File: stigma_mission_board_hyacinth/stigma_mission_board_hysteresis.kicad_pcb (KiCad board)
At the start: 4 copper layers, 70 x 120 mm, 166 parts, among them J1 DF40C-70DS-0.4V(51), J2 DF40HB(2.5)-10DS-0.4V(51), J7 SMA, J8 SMA, J9 JST-GH 4Pin, Q1 DMN2056U, Q2 DMN2056U, Q3 AOSP21321, Q8 DMN2056U, Q9 AOSP21321, U1 LAN8742A, U10 MCP2562-E-SN, U11 MCP2562-E-SN, U12 SN74HCS594, U13 INA181, U16 INA181, U2 INA181, U3 TPD4E1U06, U4 L7805, U5 L7805, U6 AZ1117H-ADJ, U7 AZ1117H-ADJ, U8 Ai-Thinker-Ra-01, U9 Ai-Thinker-Ra-01, Y1 25MHz

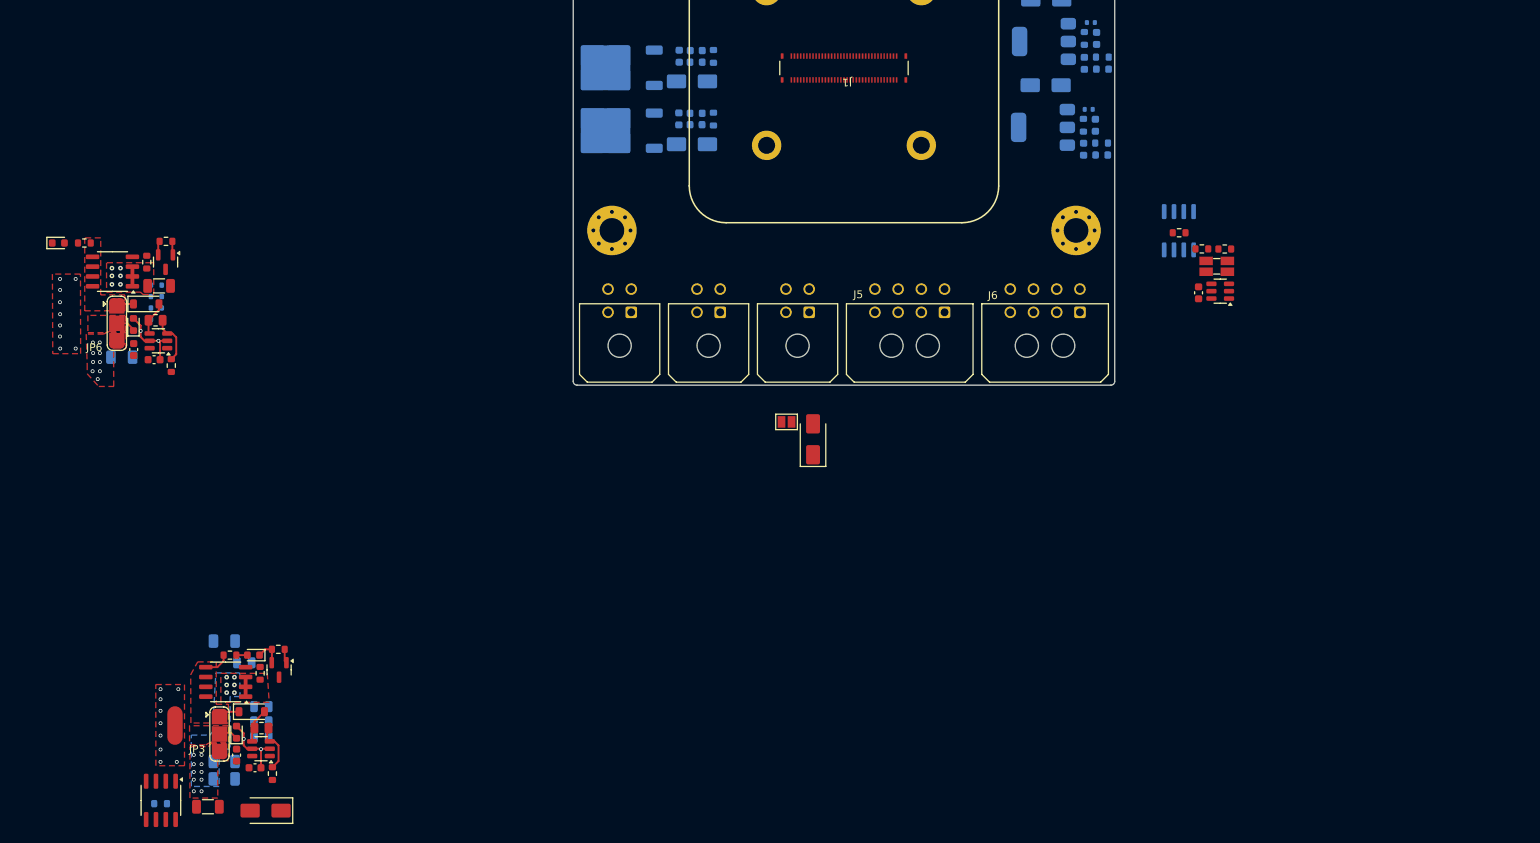
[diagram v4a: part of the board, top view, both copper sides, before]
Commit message: Rework recovery outputs to 2x2 low side
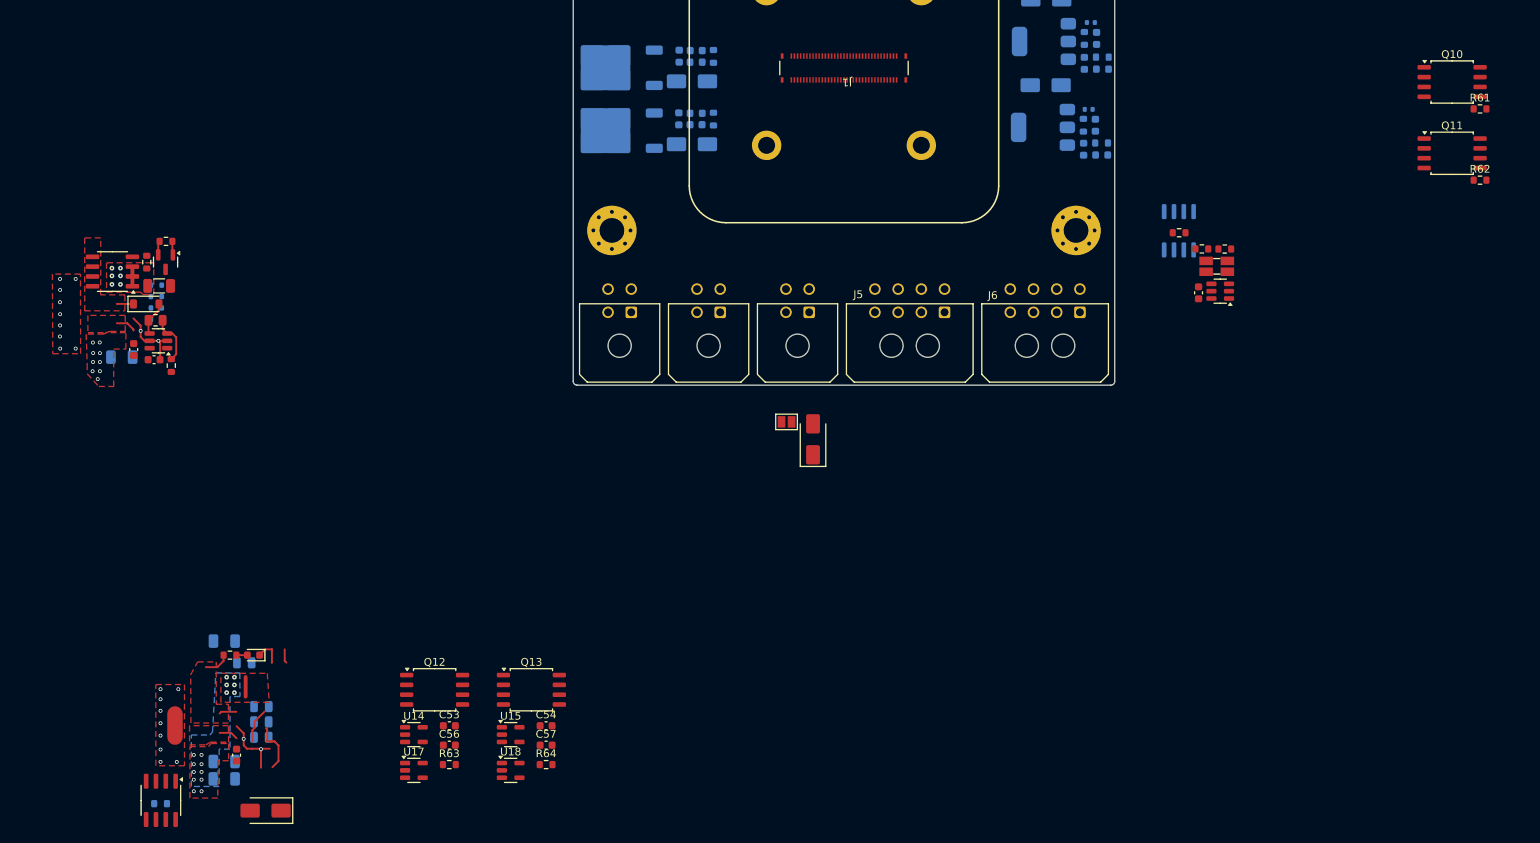
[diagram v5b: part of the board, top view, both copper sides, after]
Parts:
- removed C44: 10u, Capacitor_SMD:C_1206_3216Metric
- removed C45: 100n, Capacitor_SMD:C_0603_1608Metric
- removed D17: NRVB130T1G, Diode_SMD:D_SOD-123
- removed D19, D28: D, Diode_SMD:D_0603_1608Metric
- removed D27: LED, LED_SMD:LED_0603_1608Metric
- removed JP3, JP6: servo_switch, Stigma:SolderJumper-3_Open_RoundedPad2x2mm
- removed Q2: DMN2056U, Package_TO_SOT_SMD:SOT-23
- removed Q3: AOSP21321, Package_SO:SO-8_3.9x4.9mm_P1.27mm
- removed R45: 10k, Resistor_SMD:R_0603_1608Metric
- removed R46, R60: 1k, Resistor_SMD:R_0603_1608Metric
- removed R47: 60R, Resistor_SMD:R_0603_1608Metric
- removed Shunt1: 250mR 1%, Resistor_SMD:R_0805_2012Metric
- removed U13: INA181, Package_TO_SOT_SMD:SOT-23-6
- added C53: 100n, Capacitor_SMD:C_0603_1608Metric, F.Cu at (164.0, 291.0)
- added C54: 100n, Capacitor_SMD:C_0603_1608Metric, F.Cu at (176.5, 291.0)
- added C56: 100n, Capacitor_SMD:C_0603_1608Metric, F.Cu at (164.0, 293.5)
- added C57: 100n, Capacitor_SMD:C_0603_1608Metric, F.Cu at (176.5, 293.5)
- added Q10: TPH4R008NH, Package_SO:SSOP-8_5.25x5.24mm_P1.27mm, F.Cu at (293.6, 207.8)
- added Q11: TPH4R008NH, Package_SO:SSOP-8_5.25x5.24mm_P1.27mm, F.Cu at (293.6, 217.0)
- added Q12: TPH4R008NH, Package_SO:SSOP-8_5.25x5.24mm_P1.27mm, F.Cu at (162.1, 286.4)
- added Q13: TPH4R008NH, Package_SO:SSOP-8_5.25x5.24mm_P1.27mm, F.Cu at (174.6, 286.4)
- added R61: 10k, Resistor_SMD:R_0603_1608Metric, F.Cu at (297.2, 211.3)
- added R62: 10k, Resistor_SMD:R_0603_1608Metric, F.Cu at (297.2, 220.5)
- added R63: 10k, Resistor_SMD:R_0603_1608Metric, F.Cu at (164.0, 296.1)
- added R64: 10k, Resistor_SMD:R_0603_1608Metric, F.Cu at (176.5, 296.1)
- added U14: TF0216, Package_TO_SOT_SMD:SOT-23-5, F.Cu at (159.4, 292.2)
- added U15: TF0216, Package_TO_SOT_SMD:SOT-23-5, F.Cu at (171.9, 292.2)
- added U17: TF0216, Package_TO_SOT_SMD:SOT-23-5, F.Cu at (159.4, 296.8)
- added U18: TF0216, Package_TO_SOT_SMD:SOT-23-5, F.Cu at (171.9, 296.8)
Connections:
- net ADC_RECOVERY_1_I renamed ADC_RECOVERY
- net ADC_RECOVERY_2_I renamed RECOVERY_CONT_CHECK
- C50 pad 1: /Recovery Output 1/high_current -> high_current
- D26 pad 1: /Recovery Output 1/recovery_switched -> /recovery_high
- F1 pad 1: /Recovery Output 1/high_current -> Net-(Q12-D)
- F1 pad 2: high_current -> Net-(J10-Pin_1)
- F2 pad 1: /Recovery Output3/high_current -> Net-(Q13-D)
- F2 pad 2: high_current -> Net-(J13-Pin_1)
- F3 pad 1: /Recovery Output 1/high_current -> Net-(Q10-D)_1
- F3 pad 2: +5V -> Net-(J10-Pin_2)
- F4 pad 1: /Recovery Output3/high_current -> Net-(Q11-D)
- F4 pad 2: +5V -> Net-(J13-Pin_2)
- J1 pad 14: RECOVERY_1_CONT_CHECK -> RECOVERY_SWITCH
- J1 pad 15: RECOVERY_2_CONT_CHECK -> unconnected-(J1-Pin_15-Pad15)
- J1 pad 16: RECOVERY_3_CONT_CHECK -> unconnected-(J1-Pin_16-Pad16)
- J1 pad 17: RECOVERY_4_CONT_CHECK -> unconnected-(J1-Pin_17-Pad17)
- Q8 pad 1: RECOVERY_1 -> RECOVERY_SWITCH
- Q9 pad 1: /Recovery Output 1/high_current -> high_current
- Q9 pad 2: /Recovery Output 1/high_current -> high_current
- Q9 pad 3: /Recovery Output 1/high_current -> high_current
- Q9 pad 5: /Recovery Output 1/recovery_switched -> /recovery_high
- Q9 pad 6: /Recovery Output 1/recovery_switched -> /recovery_high
- Q9 pad 7: /Recovery Output 1/recovery_switched -> /recovery_high
- Q9 pad 8: /Recovery Output 1/recovery_switched -> /recovery_high
- R48 pad 1: /Recovery Output3/recovery_switched -> /recovery_high
- R57 pad 1: RECOVERY_1 -> RECOVERY_SWITCH
- R58 pad 1: /Recovery Output 1/high_current -> high_current
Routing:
- net (no net): track 0.00 -> 14.0 mm
- net Net-(U13-+): track 6.92 -> 0.00 mm
- net /recovery_high: track 0.00 -> 5.53 mm
- net Net-(D17-A): track 4.50 -> 0.00 mm
- net /Recovery Output 1/servo_line: track 2.63 -> 0.00 mm
- net high_current: track 0.00 -> 2.54 mm, vias 0 -> 15
- net /Recovery Output 1/high_current: track 2.54 -> 0.00 mm, vias 15 -> 0
- net /Recovery Output3/high_current: track 2.54 -> 0.00 mm, vias 16 -> 0
- net /Recovery Output3/servo_line: track 2.48 -> 0.00 mm
- net RECOVERY_SWITCH: track 0.00 -> 1.77 mm
- net RECOVERY_1: track 1.77 -> 0.00 mm
- net /Recovery Output3/recovery_switched: track 5.64 -> 4.73 mm
- net Net-(Q11-D): vias 0 -> 16
- added copper zone on F.Cu, net /recovery_high
- added copper zone on B.Cu, net Net-(Q11-D)
- added copper zone on F.Cu, net Net-(Q11-D)
- added copper zone on F.Cu, net high_current
- removed copper zone on F.Cu, net /Recovery Output 1/high_current
- removed copper zone on F.Cu, net /Recovery Output 1/recovery_switched
- removed copper zone on F.Cu, net /Recovery Output 1/servo_line
- removed copper zone on B.Cu, net /Recovery Output3/high_current
- removed copper zone on F.Cu, net /Recovery Output3/high_current
- removed copper zone on F.Cu, net /Recovery Output3/recovery_switched
- removed copper zone on F.Cu, net /Recovery Output3/servo_line

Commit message: Refactor schematic, esp. recovery outputs, prepare for final layout
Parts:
- removed C14, C15: 10u, Capacitor_SMD:C_0603_1608Metric
- removed C20, C21: 22u, Capacitor_SMD:C_0603_1608Metric
- removed C42: C, Capacitor_SMD:C_0603_1608Metric
- removed C50: 10u, Capacitor_SMD:C_1206_3216Metric
- removed D10, D9: SS34, Diode_SMD:D_SMA
- removed D11, D12: red, LED_SMD:LED_0603_1608Metric
- removed J10, J4: ~, Connector_Molex:Molex_Micro-Fit_3.0_43045-0400_2x02_P3.00mm_Horizontal
- removed JP2: SolderJumper_2_Open, Jumper:SolderJumper-2_P1.3mm_Open_Pad1.0x1.5mm
- removed R12: 100mR 1%, Resistor_SMD:R_Shunt_Ohmite_LVK12
- removed R18, R24: 10k, Resistor_SMD:R_0603_1608Metric
- removed R23: 100k, Resistor_SMD:R_0603_1608Metric
- removed R30, R32: 150R, Resistor_SMD:R_0603_1608Metric
- removed R31, R33: 310R, Resistor_SMD:R_0402_1005Metric
- removed R36, R37: 220, Resistor_SMD:R_0603_1608Metric
- removed RJ1: ~, Stigma:RJ45-TH_MJ88B-B011-RVL11-P
- removed Shunt4: 250mR 1%, Resistor_SMD:R_0805_2012Metric
- removed U6, U7: AZ1117H-ADJ, Package_TO_SOT_SMD:SOT-223-3_TabPin2
- added C37: 10u, Capacitor_SMD:C_0603_1608Metric, F.Cu at (357.9, 347.4)
- added C38: 22u, Capacitor_SMD:C_0603_1608Metric, F.Cu at (357.9, 349.9)
- added C39: 10u, Capacitor_SMD:C_0603_1608Metric, F.Cu at (418.7, 66.9)
- added C44: 10u, Capacitor_SMD:C_0603_1608Metric, F.Cu at (162.1, 106.6)
- added C45: 10u, Capacitor_SMD:C_0603_1608Metric, F.Cu at (275.2, 128.8)
- added C46: 22u, Capacitor_SMD:C_0603_1608Metric, F.Cu at (175.2, 119.3)
- added C47: 22u, Capacitor_SMD:C_0603_1608Metric, F.Cu at (263.9, 121.6)
- added C58: 100n, Capacitor_SMD:C_0603_1608Metric, F.Cu at (30.3, 195.4)
- added C59: 100n, Capacitor_SMD:C_0603_1608Metric, F.Cu at (290.7, 260.0)
- added C60: 100n, Capacitor_SMD:C_0603_1608Metric, F.Cu at (290.7, 262.5)
- added C61: 100n, Capacitor_SMD:C_0603_1608Metric, F.Cu at (290.7, 265.1)
- added C62: 100n, Capacitor_SMD:C_0603_1608Metric, F.Cu at (290.7, 267.6)
- added D21: red, LED_SMD:LED_0603_1608Metric, F.Cu at (139.2, 309.7)
- added D22: red, LED_SMD:LED_0603_1608Metric, F.Cu at (139.2, 312.3)
- added F5: PTC?, Fuse:Fuse_1206_3216Metric, F.Cu at (144.8, 302.4)
- added J11: JST-GH, Connector_JST:JST_GH_BM04B-GHS-TBT_1x04-1MP_P1.25mm_Vertical, F.Cu at (407.1, 286.2)
- added J3: RJ45_Wuerth_7499010211A, Connector_RJ:RJ45_Wuerth_7499010211A_Horizontal, F.Cu at (218.5, 137.2)
- added R56: 10k, Resistor_SMD:R_0603_1608Metric, F.Cu at (144.8, 314.0)
- added R60: 1k, Resistor_SMD:R_0603_1608Metric, F.Cu at (42.4, 205.5)
- added R65: 220, Resistor_SMD:R_0603_1608Metric, F.Cu at (42.4, 208.0)
- added R66: 1k, Resistor_SMD:R_0603_1608Metric, F.Cu at (42.4, 210.5)
- added R67: 220, Resistor_SMD:R_0603_1608Metric, F.Cu at (42.4, 213.0)
- added R68: 1k, Resistor_SMD:R_0603_1608Metric, F.Cu at (42.4, 215.5)
- added R69: 10k, Resistor_SMD:R_0603_1608Metric, F.Cu at (46.4, 185.4)
- added R70: 22, Resistor_SMD:R_0603_1608Metric, F.Cu at (415.2, 272.0)
- added R71: 270, Resistor_SMD:R_0603_1608Metric, F.Cu at (452.4, 50.3)
- added R72: 22, Resistor_SMD:R_0603_1608Metric, F.Cu at (415.2, 277.0)
- added R73: 22, Resistor_SMD:R_0603_1608Metric, F.Cu at (415.2, 279.5)
- added R74: 22, Resistor_SMD:R_0603_1608Metric, F.Cu at (415.2, 282.0)
- added U13: AZ1117I-3.3, Package_TO_SOT_SMD:SOT-223-3_TabPin2, F.Cu at (407.8, 55.6)
- added U19: AZ1117I-3.3, Package_TO_SOT_SMD:SOT-223-3_TabPin2, F.Cu at (157.5, 114.8)
- added U20: AZ1117I-3.3, Package_TO_SOT_SMD:SOT-223-3_TabPin2, F.Cu at (263.9, 131.8)
- C16, C17, C18, C19, C31, C33, C34, C52, D1, D2, D3, D4, D5, D6, D7, D8, F1, F2, F3, F4, R41, U4, U5: moved to F.Cu
- C43: value 100n -> 22u
- D18: value LED -> yellow
- J13: footprint Connector_Molex:Molex_Micro-Fit_3.0_43045-0400_2x02_P3.00mm_Horizontal -> Connector_Molex:Molex_Micro-Fit_3.0_43045-1200_2x06_P3.00mm_Horizontal
- J9: value JST-GH 4Pin -> JST-GH
- R1, R2, R4: value 33R -> 33
- R28: value 270 -> 100k
- R34, R35: value 220 -> 1k; moved to F.Cu
- R42: value R -> 10k
- R44: value @todo -> 220
- R48: value 1k -> 10k
- R59: value 60R -> 1k
- U10: value MCP2562-E-SN -> MCP2562; moved to F.Cu
- U11: value MCP2562-E-SN -> MCP2562
- U12: value SN74HCS594 -> AZ1117I-3.3; footprint Package_SO:TSSOP-16_4.4x5mm_P0.65mm -> Package_TO_SOT_SMD:SOT-223-3_TabPin2
- moved C43 289.5 mm to (418.7, 69.4), turned to 0 degrees
- moved U12 287.2 mm to (346.9, 332.8)
- moved Q10 235.8 mm to (58.6, 187.5)
- moved Q11 235.2 mm to (58.6, 206.1)
- moved R61 232.3 mm to (65.9, 190.4)
- moved R62 231.6 mm to (65.9, 209.0)
- moved C40 213.7 mm to (123.2, 324.1)
- moved C35 212.8 mm to (128.7, 316.5)
- moved Q1 209.5 mm to (445.1, 209.2), turned to 0 degrees
- moved R28 209.4 mm to (201.2, 323.2), turned to 0 degrees
- moved C32 207.0 mm to (123.2, 315.1)
- moved R44 206.6 mm to (443.1, 204.4), turned to 0 degrees
- moved D16 203.9 mm to (439.0, 210.3), turned to 0 degrees
- moved R43 203.3 mm to (443.1, 201.9)
- moved C30 203.3 mm to (123.2, 309.1)
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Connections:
- net CAN_1_RX renamed CAN1_RX
- net CAN_1_TX renamed CAN1_TX
- net CAN_2_RX renamed CAN2_RX
- net CAN_2_TX renamed CAN2_TX
- net ETH_TXD0 renamed ETH_TXD-
- net ETH_TXD1 renamed ETH_TXD+
- net HSE_IN renamed Net-(U1-XTAL1/CLKIN)
- net HSE_OUT renamed Net-(U1-XTAL2)
- net LoRa_1_BUSY renamed LORA1_BUSY
- net LoRa_1_IRQ renamed LORA1_IRQ
- net LoRa_1_NSS renamed LORA1_CS
- net LoRa_2_BUSY renamed LORA2_BUSY
- net LoRa_2_IRQ renamed LORA2_IRQ
- net RECOVERY_1 renamed RECOVERY_LOW1
- net RECOVERY_1_CONT_CHECK renamed Net-(Q2-S)
- net RECOVERY_2 renamed RECOVERY_LOW2
- net RECOVERY_3 renamed RECOVERY_LOW3
- net RECOVERY_4 renamed RECOVERY_LOW4
- net TELEMETRIE_SPI4_MISO renamed LORA_SPI4_MISO
- net TELEMETRIE_SPI4_MOSI renamed LORA_SPI4_MOSI
- net TELEMETRIE_SPI4_SCK renamed LORA_SPI4_SCK
- C16 pad 2: main_voltage -> main
- C17 pad 2: main_voltage -> main
- C26 pad 2: +3.3V -> vdd_lora1
- C27 pad 2: +3.3V -> vdd_lora2
- C28 pad 2: +3.3V -> vdd_lora1
- C29 pad 2: +3.3V -> vdd_lora2
- C3 pad 1: +3.3V -> vdd_ethernet
- C30 pad 2: main_voltage -> main
- C31 pad 2: high_current -> recovery
- C32 pad 2: main_voltage -> main
- C33 pad 2: high_current -> recovery
- C34 pad 2: high_current -> recovery
- C35 pad 2: main_voltage -> main
- C36 pad 2: high_current -> recovery
- C40 pad 2: main_voltage -> main
- C43 pad 2: +3.3V -> vdd_ethernet
- C51 pad 1: +3.3V -> GND
- C51 pad 2: GND -> +3.3V
- C52 pad 2: high_current -> recovery
- C55 pad 2: high_current -> recovery
- D14 pad 1: v_main_pre_sense -> main_pre_sense
- D14 pad 2: Net-(D14-A) -> bus_main
- D15 pad 1: v_main_pre_sense -> main_pre_sense
- D15 pad 2: Net-(D15-A) -> recovery
- D26 pad 1: /recovery_high -> Net-(D26-K)
- D3 pad 1: SR_GPS_RESET -> GPS_RESET
- D4 pad 1: SR_GPS_SAFEBOOT -> GPS_SAFEBOOT
- F1 pad 1: Net-(Q12-D) -> Net-(D19-K)
- F1 pad 2: Net-(J10-Pin_1) -> Net-(Q12-D)
- F2 pad 1: Net-(Q13-D) -> Net-(D20-K)
- F2 pad 2: Net-(J13-Pin_1) -> Net-(Q13-D)
- FB1 pad 1: +3.3V -> vdd_ethernet
- J1 pad 11: SR1_SER -> LORA1_RESET
- J1 pad 12: SR1_SRCLK -> LORA2_CS
- J1 pad 13: SR1_RCLK -> LORA2_RESET
- J1 pad 14: RECOVERY_SWITCH -> GPS_RESET
- J1 pad 15: unconnected-(J1-Pin_15-Pad15) -> GPS_SAFEBOOT
- J1 pad 16: unconnected-(J1-Pin_16-Pad16) -> RECOVERY_HIGH
- J1 pad 17: unconnected-(J1-Pin_17-Pad17) -> CONT_CHECK
- J1 pad 23: SPI3_SCK_PC10 -> unconnected-(J1-Pin_23-Pad23)
- J1 pad 24: SPI3_MISO_PC11 -> unconnected-(J1-Pin_24-Pad24)
- J1 pad 25: SPI3_MOSI_PC12 -> unconnected-(J1-Pin_25-Pad25)
- J1 pad 28: ADC_HIGH_CURRENT -> ADC_IN
- J1 pad 29: ADC_HIGH_CURRENT2 -> ETH_RESET
- J1 pad 4: LoRa_2_NSS -> UART8_RX
- J1 pad 46: ADC_RECOVERY -> ADC_BUS_MAIN_VOLTAGE
- J1 pad 47: RECOVERY_CONT_CHECK -> ADC_BUS_SUPPLY_VOLTAGE
- J1 pad 5: ETH_nINT -> UART8_TX
- J1 pad 59: ADC_RECOVERY_3_I -> ADC_MAIN_CURRENT
- J1 pad 62: ADC_RECOVERY_4_I -> ADC_RECOVERY_VOLTAGE
- J1 pad 65: ADC_MAIN_VOLTAGE_CURRENT -> ADC_RECOVERY_CURRENT
- J1 pad 67: ADC_MAIN_VOLTAGE -> ADC_CONT_CHECK
- J2 pad 6: SR_GPS_SAFEBOOT -> GPS_SAFEBOOT
- J2 pad 7: SR_GPS_RESET -> GPS_RESET
- J9 pad 2: DAC -> Net-(J9-Pin_2)
- J9 pad 3: GND -> Net-(J9-Pin_3)
- Q8 pad 1: RECOVERY_SWITCH -> Net-(Q8-G)
- Q9 pad 1: high_current -> recovery
- Q9 pad 2: high_current -> recovery
- Q9 pad 3: high_current -> recovery
- Q9 pad 5: /recovery_high -> Net-(D26-K)
- Q9 pad 6: /recovery_high -> Net-(D26-K)
- Q9 pad 7: /recovery_high -> Net-(D26-K)
- Q9 pad 8: /recovery_high -> Net-(D26-K)
- R1 pad 2: ETH_RXD0 -> ETH_RXD-
- R10 pad 2: +3.3V -> vdd_ethernet
- R11 pad 2: +3.3V -> vdd_ethernet
- R19 pad 1: v_main_pre_sense -> bus_main
- R19 pad 2: ADC_MAIN_VOLTAGE -> ADC_BUS_MAIN_VOLTAGE
- R2 pad 2: ETH_RXD1 -> ETH_RXD+
- R20 pad 1: ADC_MAIN_VOLTAGE -> ADC_BUS_MAIN_VOLTAGE
- R22 pad 1: ETH_nINT -> Net-(U1-LED2/~{INTSEL})
- R25 pad 1: high_current -> bus_supply
- R25 pad 2: ADC_HIGH_CURRENT -> ADC_BUS_SUPPLY_VOLTAGE
- R26 pad 1: ADC_HIGH_CURRENT -> ADC_BUS_SUPPLY_VOLTAGE
- R28 pad 1: Net-(RJ1-L-) -> recovery
- R28 pad 2: GND -> ADC_RECOVERY_VOLTAGE
- R40 pad 1: CAN_1_H -> CAN1+
- R40 pad 2: CAN_1_L -> CAN1-
- R41 pad 1: CAN_2_H -> CAN2+
- R41 pad 2: CAN_2_L -> CAN2-
- R42 pad 1: +3.3V -> ADC_RECOVERY_VOLTAGE
- R42 pad 2: Net-(U12-~{RCLR}) -> GND
- R48 pad 1: /recovery_high -> /Recovery Output 1 & 2/recovery_high
- R57 pad 1: RECOVERY_SWITCH -> recovery
- R57 pad 2: GND -> Net-(D22-A)
- R58 pad 1: high_current -> recovery
- R59 pad 2: Net-(U16-+) -> Net-(R59-Pad2)
- R6 pad 1: SR_ETH_RESET -> Net-(U1-~{INT}/REFCLKO)
- R6 pad 2: +3.3V -> vdd_ethernet
- R8 pad 2: +3.3V -> vdd_ethernet
- R9 pad 2: +3.3V -> vdd_ethernet
- U1 pad 15: SR_ETH_RESET -> ETH_RESET
- U1 pad 2: ETH_nINT -> Net-(U1-LED2/~{INTSEL})
- U1 pad 9: +3.3V -> vdd_ethernet
- U10 pad 6: CAN_1_L -> CAN1-
- U10 pad 7: CAN_1_H -> CAN1+
- U10 pad 8: SR_CAN_STBY_1 -> GND
- U11 pad 6: CAN_2_L -> CAN2-
- U11 pad 7: CAN_2_H -> CAN2+
- U11 pad 8: SR_CAN_STBY_2 -> GND
- U12 pad 1: SR_CAN_STBY_2 -> GND
- U12 pad 2: SR_ETH_RESET -> +3.3V
- U12 pad 3: SR_LoRa_1_RESET -> +5V
- U16 pad 1: ADC_RECOVERY -> ADC_RECOVERY_CURRENT
- U16 pad 3: Net-(U16-+) -> Net-(D26-K)
- U16 pad 4: Net-(D26-A) -> /Recovery Output 1 & 2/recovery_high
- U2 pad 1: ADC_MAIN_VOLTAGE_CURRENT -> ADC_MAIN_CURRENT
- U2 pad 3: Net-(U2-+) -> main_pre_sense
- U2 pad 4: Net-(U2--) -> main
- U3 pad 4: /RXP -> /RXN
- U3 pad 5: /RXN -> /RXP
- U4 pad 1: main_voltage -> main
- U5 pad 1: main_voltage -> main
- U8 pad 3: +3.3V -> vdd_lora1
- U8 pad 4: SR_LoRa_1_RESET -> LORA1_RESET
- U9 pad 15: LoRa_2_NSS -> LORA2_CS
- U9 pad 3: +3.3V -> vdd_lora2
- U9 pad 4: SR_LoRa_2_RESET -> LORA2_RESET
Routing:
- net GND: track 26.5 -> 0.00 mm, vias 22 -> 0
- net (no net): track 14.0 -> 0.00 mm
- net Net-(U16-+): track 6.41 -> 0.00 mm
- net /recovery_high: track 5.53 -> 0.00 mm
- net /Recovery Output3/recovery_switched: track 4.73 -> 0.00 mm
- net Net-(D26-A): track 4.44 -> 0.00 mm
- net /Recovery Output 1/recovery_switched: track 2.63 -> 0.00 mm
- net high_current: track 2.54 -> 0.00 mm, vias 15 -> 0
- net RECOVERY_LOW3: track 1.82 -> 0.00 mm
- net RECOVERY_SWITCH: track 1.77 -> 0.00 mm
- net Net-(D18-A): track 1.43 -> 0.00 mm
- net Net-(Q11-D): vias 16 -> 0
- removed copper zone on F.Cu, net /recovery_high
- removed copper zone on F.Cu, net GND
- removed copper zone on B.Cu, net Net-(Q11-D)
- removed copper zone on F.Cu, net Net-(Q11-D)
- removed copper zone on F.Cu, net high_current
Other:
- outline, holes or cut-outs redrawn
- board text removed: "3,3V"
- board text removed: "5V Regulator"
- board text removed: "BZR"
- board text removed: "Ethernet"
- board text removed: "see what we do with those"
- board text removed: "sensing"
- board text removed: "shift"

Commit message: start routing
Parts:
- removed C56, C57, C58, C59, C60, C61, C62: 100n, Capacitor_SMD:C_0603_1608Metric
- removed D14: SS34, Diode_SMD:D_SMA
- removed D21, D22: red, LED_SMD:LED_0603_1608Metric
- removed D26: NRVB130T1G, Diode_SMD:D_SOD-123
- removed J11: JST-GH, Connector_JST:JST_GH_BM04B-GHS-TBT_1x04-1MP_P1.25mm_Vertical
- removed J13: ~, Connector_Molex:Molex_Micro-Fit_3.0_43045-1200_2x06_P3.00mm_Horizontal
- removed Q10, Q11, Q12, Q13: TPH4R008NH, Package_SO:SSOP-8_5.25x5.24mm_P1.27mm
- removed Q9: AOSP21321, Package_SO:SO-8_3.9x4.9mm_P1.27mm
- removed R67: 220, Resistor_SMD:R_0603_1608Metric
- removed R68: 1k, Resistor_SMD:R_0603_1608Metric
- removed R69: 10k, Resistor_SMD:R_0603_1608Metric
- removed R70, R72, R73, R74: 22, Resistor_SMD:R_0603_1608Metric
- removed R71: 270, Resistor_SMD:R_0603_1608Metric
- removed U19, U20: AZ1117I-3.3, Package_TO_SOT_SMD:SOT-223-3_TabPin2
- added C14: 100n, Capacitor_SMD:C_0402_1005Metric, F.Cu at (204.3, 222.3)
- added C15: 10u, Capacitor_SMD:C_0603_1608Metric, F.Cu at (165.3, 172.5)
- added C20: 1u, Capacitor_SMD:C_0402_1005Metric, F.Cu at (192.9, 235.0)
- added C21: 10u, Capacitor_SMD:C_0603_1608Metric, F.Cu at (160.5, 233.2)
- added C41: 1u, Capacitor_SMD:C_0402_1005Metric, F.Cu at (176.0, 179.5)
- added C42: 470p, Capacitor_SMD:C_0402_1005Metric, F.Cu at (176.0, 178.6)
- added C48: 10u, Capacitor_SMD:C_0603_1608Metric, F.Cu at (253.3, 102.4)
- added C49: 100n, Capacitor_SMD:C_0402_1005Metric, F.Cu at (265.9, 131.5)
- added C50: 10p, Capacitor_SMD:C_0402_1005Metric, F.Cu at (177.7, 183.0)
- added D10: yellow, LED_SMD:LED_0603_1608Metric, F.Cu at (181.5, 222.5)
- added D17: yellow, LED_SMD:LED_0603_1608Metric, F.Cu at (168.2, 270.8)
- added D19: yellow, LED_SMD:LED_0603_1608Metric, F.Cu at (171.7, 271.1)
- added D9: SS34, Diode_SMD:D_SMA, F.Cu at (177.7, 217.7)
- added J10: JST-GH, Connector_JST:JST_GH_SM04B-GHS-TB_1x04-1MP_P1.25mm_Horizontal, F.Cu at (174.1, 201.3)
- added J4: ~, Connector_Molex:Molex_Micro-Fit_3.0_43045-0800_2x04_P3.00mm_Horizontal, F.Cu at (208.1, 238.2)
- added JP1: Jumper_3_Open, Connector_PinHeader_2.54mm:PinHeader_1x03_P2.54mm_Vertical, F.Cu at (168.9, 276.7)
- added JP2: Jumper_3_Open, Connector_PinHeader_2.54mm:PinHeader_1x03_P2.54mm_Vertical, F.Cu at (181.2, 274.3)
- added JP3: Jumper_2_Small_Open, Connector_PinHeader_2.54mm:PinHeader_1x02_P2.54mm_Vertical, F.Cu at (227.2, 209.8)
- added JP4: Jumper_2_Small_Open, Connector_PinHeader_2.54mm:PinHeader_1x02_P2.54mm_Vertical, F.Cu at (227.3, 219.2)
- added Q2: AO3400A, Package_TO_SOT_SMD:SOT-23, F.Cu at (199.1, 229.7)
- added Q3: AO3401A, Package_TO_SOT_SMD:SOT-23, F.Cu at (173.1, 217.4)
- added Q4: AO3400A, Package_TO_SOT_SMD:SOT-23, F.Cu at (222.7, 184.7)
- added Q5: TPH4R008NH, Package_SO:SSOP-8_5.25x5.24mm_P1.27mm, B.Cu at (199.1, 228.7)
- added Q6: TPH4R008NH, Package_SO:SSOP-8_5.25x5.24mm_P1.27mm, B.Cu at (193.3, 228.7)
- added Q7: TPH4R008NH, Package_SO:SSOP-8_5.25x5.24mm_P1.27mm, B.Cu at (187.5, 228.7)
- added R12: 1k, Resistor_SMD:R_0402_1005Metric, F.Cu at (196.3, 226.5)
- added R18: 220, Resistor_SMD:R_0402_1005Metric, F.Cu at (172.2, 215.1)
- added R23: 10k, Resistor_SMD:R_0402_1005Metric, F.Cu at (173.7, 220.1)
- added R24: 0, Resistor_SMD:R_0402_1005Metric, F.Cu at (248.5, 129.6)
- added R30: 50R, Resistor_SMD:R_0402_1005Metric, F.Cu at (153.1, 133.5)
- added R31: 50R, Resistor_SMD:R_0402_1005Metric, F.Cu at (153.1, 135.5)
- added R32: 50R, Resistor_SMD:R_0402_1005Metric, F.Cu at (153.1, 137.5)
- added R33: 50R, Resistor_SMD:R_0402_1005Metric, F.Cu at (156.8, 130.2)
- added R36: 33, Resistor_SMD:R_0402_1005Metric, F.Cu at (185.9, 191.2)
- added R37: 10k, Resistor_SMD:R_0402_1005Metric, F.Cu at (180.4, 181.2)
- added R45: 270, Resistor_SMD:R_0402_1005Metric, F.Cu at (175.2, 149.3)
- added R46: 10k, Resistor_SMD:R_0402_1005Metric, F.Cu at (175.2, 151.3)
- added R47: 270, Resistor_SMD:R_0402_1005Metric, F.Cu at (175.2, 153.3)
- added R49: 0, Resistor_SMD:R_0402_1005Metric, F.Cu at (177.7, 181.1)
- added R50: 0, Resistor_SMD:R_0402_1005Metric, F.Cu at (173.9, 178.8)
- added R51: 22, Resistor_SMD:R_0402_1005Metric, F.Cu at (178.3, 200.8)
- added R52: 22, Resistor_SMD:R_0402_1005Metric, F.Cu at (178.3, 201.8)
- added R53: 10k, Resistor_SMD:R_0402_1005Metric, F.Cu at (176.7, 268.2)
- added R54: 220, Resistor_SMD:R_0402_1005Metric, F.Cu at (180.9, 261.0)
- added R55: 10k, Resistor_SMD:R_0402_1005Metric, F.Cu at (180.9, 262.9)
- added U6: AZ1117I-3.3, Package_TO_SOT_SMD:SOT-223-3_TabPin2, B.Cu at (168.2, 168.8)
- added U7: AZ1117I-3.3, Package_TO_SOT_SMD:SOT-223-3_TabPin2, F.Cu at (278.0, 125.9)
- C1: value 10u -> 330n; footprint Capacitor_SMD:C_1206_3216Metric -> Capacitor_SMD:C_0402_1005Metric
- C10, C18, C3, C8: value 100n -> 22u
- C11, C2, C28, C29, C53, C54: footprint Capacitor_SMD:C_0603_1608Metric -> Capacitor_SMD:C_0402_1005Metric
- C12: value 10p -> 330n
- C13: value 10p -> 100n
- C16: value 330n -> 22u
- C17: value 330n -> 10u
- C19: value 100n -> 1u; footprint Capacitor_SMD:C_0603_1608Metric -> Capacitor_SMD:C_0402_1005Metric
- C22, C23: value DNP -> 22u
- C24: value DNP -> 4u7
- C25: value DNP -> 100n; footprint Capacitor_SMD:C_0603_1608Metric -> Capacitor_SMD:C_0402_1005Metric
- C26, C27: value 10u -> 100n; footprint Capacitor_SMD:C_1206_3216Metric -> Capacitor_SMD:C_0402_1005Metric
- C30, C31: value 22u -> 100n; footprint Capacitor_SMD:C_0805_2012Metric -> Capacitor_SMD:C_0402_1005Metric
- C32, C33: value 10u -> DNP; footprint Capacitor_SMD:C_0805_2012Metric -> Capacitor_SMD:C_0603_1608Metric
- C34: value 22u -> 10u; footprint Capacitor_SMD:C_0805_2012Metric -> Capacitor_SMD:C_0603_1608Metric
- C35, C36, C55: value 1u -> 100n; footprint Capacitor_SMD:C_0603_1608Metric -> Capacitor_SMD:C_0402_1005Metric
- C37, C39, C44, C45: value 10u -> 100n; footprint Capacitor_SMD:C_0603_1608Metric -> Capacitor_SMD:C_0402_1005Metric
- C38: value 22u -> 100n; footprint Capacitor_SMD:C_0603_1608Metric -> Capacitor_SMD:C_0402_1005Metric
- C4, C9: value 100n -> 10u
- C40, C52: value 4u7 -> 100n; footprint Capacitor_SMD:C_0805_2012Metric -> Capacitor_SMD:C_0402_1005Metric
- C43: value 22u -> 10u
- C46, C47: value 22u -> DNP
- C5: footprint Capacitor_SMD:C_1206_3216Metric -> Capacitor_SMD:C_0402_1005Metric
- C51: value 100n -> 10p; footprint Capacitor_SMD:C_0603_1608Metric -> Capacitor_SMD:C_0402_1005Metric
- C6: value 100n -> 4u7
- C7: value 470p -> 10u; footprint Capacitor_SMD:C_0402_1005Metric -> Capacitor_SMD:C_0603_1608Metric
- D1, D2, D3: value ESD5Zxx -> SS34; footprint Diode_SMD:D_SOD-523 -> Diode_SMD:D_SMA
- D16: value ~ -> yellow; footprint Diode_SMD:D_SOD-123F -> LED_SMD:LED_0603_1608Metric
- D4: value ESD5Zxx -> red; footprint Diode_SMD:D_SOD-523 -> LED_SMD:LED_0603_1608Metric
- D5, D6: value SS34 -> red; footprint Diode_SMD:D_SMA -> LED_SMD:LED_0603_1608Metric
- D7: value red -> SS34; footprint LED_SMD:LED_0603_1608Metric -> Diode_SMD:D_SMA
- F1: value 10A -> PTC?
- F5: value PTC? -> 10A
- FB1: footprint Resistor_SMD:R_0603_1608Metric -> Inductor_SMD:L_0603_1608Metric
- J3: value RJ45_Wuerth_7499010211A -> ~; footprint Connector_RJ:RJ45_Wuerth_7499010211A_Horizontal -> Connector_Molex:Molex_Micro-Fit_3.0_43045-0800_2x04_P3.00mm_Horizontal
- J5: footprint Connector_Molex:Molex_Micro-Fit_3.0_43045-0800_2x04_P3.00mm_Horizontal -> Connector_Molex:Molex_Micro-Fit_3.0_43045-1200_2x06_P3.00mm_Horizontal
- J6: value ~ -> SMA; footprint Connector_Molex:Molex_Micro-Fit_3.0_43045-0800_2x04_P3.00mm_Horizontal -> Connector_Coaxial:SMA_Amphenol_132289_EdgeMount
- J7: footprint Connector_Coaxial:SMA_Amphenol_901-143_Horizontal -> Connector_Coaxial:SMA_Amphenol_132289_EdgeMount
- J8: value SMA -> RJ45_Wuerth_7499010211A; footprint Connector_Coaxial:SMA_Amphenol_901-143_Horizontal -> Connector_RJ:RJ45_Wuerth_7499010211A_Horizontal
- J9: footprint Connector_JST:JST_GH_BM04B-GHS-TBT_1x04-1MP_P1.25mm_Vertical -> Connector_JST:JST_GH_SM04B-GHS-TB_1x04-1MP_P1.25mm_Horizontal
- Q1: value DMN2056U -> TPH1R712MD; footprint Package_TO_SOT_SMD:SOT-23 -> Package_SO:SSOP-8_5.25x5.24mm_P1.27mm
- Q8: value DMN2056U -> TPH4R008NH; footprint Package_TO_SOT_SMD:SOT-23 -> Package_SO:SSOP-8_5.25x5.24mm_P1.27mm; moved to B.Cu
- R1: value 33 -> 100m, 1%; footprint Resistor_SMD:R_0603_1608Metric -> Resistor_SMD:R_2512_6332Metric
- R10, R39, R44, R48, R57, R6, R62, R64, R65, R9: footprint Resistor_SMD:R_0603_1608Metric -> Resistor_SMD:R_0402_1005Metric
- R11, R20: value 10k -> 1k; footprint Resistor_SMD:R_0603_1608Metric -> Resistor_SMD:R_0402_1005Metric
- R13: value 50R -> 120; footprint Resistor_SMD:R_0603_1608Metric -> Resistor_SMD:R_0402_1005Metric
- R14: value 50R -> 220; footprint Resistor_SMD:R_0603_1608Metric -> Resistor_SMD:R_0402_1005Metric
- R15: value 12.1k -> 1k; footprint Resistor_SMD:R_0603_1608Metric -> Resistor_SMD:R_0402_1005Metric
- R16: value 50R -> 1k; footprint Resistor_SMD:R_0603_1608Metric -> Resistor_SMD:R_0402_1005Metric
- R17: value 50R -> 250m, 1%; footprint Resistor_SMD:R_0603_1608Metric -> Resistor_SMD:R_2512_6332Metric
- R19, R25, R28: value 100k -> 10k; footprint Resistor_SMD:R_0603_1608Metric -> Resistor_SMD:R_0402_1005Metric
- R2, R4: value 33 -> 100k; footprint Resistor_SMD:R_0603_1608Metric -> Resistor_SMD:R_0402_1005Metric
- R21: value 0 -> 1k
- R22: value 10k -> 120; footprint Resistor_SMD:R_0603_1608Metric -> Resistor_SMD:R_0402_1005Metric
- R26: value 10k -> 1k5; footprint Resistor_SMD:R_0603_1608Metric -> Resistor_SMD:R_0402_1005Metric
- R27: value 0 -> 10k
- R29: value 270 -> 10k; footprint Resistor_SMD:R_0603_1608Metric -> Resistor_SMD:R_0402_1005Metric
- R3: value 10k -> 100k; footprint Resistor_SMD:R_0603_1608Metric -> Resistor_SMD:R_0402_1005Metric
- R34: value 1k -> 0; footprint Resistor_SMD:R_0603_1608Metric -> Resistor_SMD:R_0402_1005Metric
- R35: value 1k -> 33; footprint Resistor_SMD:R_0603_1608Metric -> Resistor_SMD:R_0402_1005Metric
- R38: value 0 -> 33; footprint Resistor_SMD:R_0603_1608Metric -> Resistor_SMD:R_0402_1005Metric
- R40: value 120, DNP -> 12.1k; footprint Resistor_SMD:R_0603_1608Metric -> Resistor_SMD:R_0402_1005Metric
- R41: value 120, DNP -> 22; footprint Resistor_SMD:R_0603_1608Metric -> Resistor_SMD:R_0402_1005Metric
- R42: value 10k -> 22; footprint Resistor_SMD:R_0603_1608Metric -> Resistor_SMD:R_0402_1005Metric
- R43: value 10k -> 33R; footprint Resistor_SMD:R_0603_1608Metric -> Resistor_SMD:R_0402_1005Metric
- R5: value 0 -> 1k; footprint Resistor_SMD:R_0603_1608Metric -> Resistor_SMD:R_0402_1005Metric
- R56, R61, R63: value 10k -> 220; footprint Resistor_SMD:R_0603_1608Metric -> Resistor_SMD:R_0402_1005Metric
- R58: value 1k -> 220; footprint Resistor_SMD:R_0603_1608Metric -> Resistor_SMD:R_0402_1005Metric
- R59, R60, R66: value 1k -> 10k; footprint Resistor_SMD:R_0603_1608Metric -> Resistor_SMD:R_0402_1005Metric
- R7: value 33R -> 10k; footprint Resistor_SMD:R_0603_1608Metric -> Resistor_SMD:R_0402_1005Metric
- R8: value 1k5 -> 10k; footprint Resistor_SMD:R_0603_1608Metric -> Resistor_SMD:R_0402_1005Metric
- U1: value LAN8742A -> L7805; footprint Package_DFN_QFN:VQFN-24-1EP_4x4mm_P0.5mm_EP2.5x2.5mm_ThermalVias -> Package_TO_SOT_SMD:TO-252-2; moved to B.Cu
- U11: value MCP2562 -> Ai-Thinker-Ra-01; footprint Package_SO:SOIC-8_3.9x4.9mm_P1.27mm -> RF_Module:Ai-Thinker-Ra-01-LoRa; moved to B.Cu
- U12: value AZ1117I-3.3 -> TPD4E1U06; footprint Package_TO_SOT_SMD:SOT-223-3_TabPin2 -> Package_TO_SOT_SMD:SOT-563
- U13: value AZ1117I-3.3 -> Ai-Thinker-Ra-01; footprint Package_TO_SOT_SMD:SOT-223-3_TabPin2 -> RF_Module:Ai-Thinker-Ra-01-LoRa; moved to B.Cu
- U14: value TF0216 -> LAN8742A; footprint Package_TO_SOT_SMD:SOT-23-5 -> Package_DFN_QFN:VQFN-24-1EP_4x4mm_P0.5mm_EP2.5x2.5mm_ThermalVias
- U16: value INA181 -> TF0216; footprint Package_TO_SOT_SMD:SOT-23-6 -> Package_TO_SOT_SMD:SOT-23-5
- U2: value INA181 -> AZ1117I-3.3; footprint Package_TO_SOT_SMD:SOT-23-6 -> Package_TO_SOT_SMD:SOT-223-3_TabPin2; moved to B.Cu
- U3: value TPD4E1U06 -> AZ1117I-3.3; footprint Package_TO_SOT_SMD:SOT-563 -> Package_TO_SOT_SMD:SOT-223-3_TabPin2
- U4: value L7805 -> INA181A4; footprint Package_TO_SOT_SMD:TO-252-2 -> Package_TO_SOT_SMD:SOT-23-6
- U5: moved to B.Cu
- U8: value Ai-Thinker-Ra-01 -> MCP2562; footprint RF_Module:Ai-Thinker-Ra-01-LoRa -> Package_SO:SOIC-8_3.9x4.9mm_P1.27mm; moved to F.Cu
- U9: value Ai-Thinker-Ra-01 -> INA181A4; footprint RF_Module:Ai-Thinker-Ra-01-LoRa -> Package_TO_SOT_SMD:SOT-23-6; moved to F.Cu
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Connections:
- C1 pad 1: Net-(J3-CRD) -> GND
- C1 pad 2: GND -> main
- C10 pad 1: Net-(J3-CRD) -> GND
- C10 pad 2: GND -> vdd_lora1
- C11 pad 1: +3.3V -> ADC_MAIN_CURRENT
- C12 pad 2: Net-(C12-Pad2) -> main
- C13 pad 2: Net-(C13-Pad2) -> Net-(D7-A)
- C16 pad 2: main -> vdd_ethernet
- C17 pad 2: main -> +5V
- C18 pad 2: Net-(D5-A) -> vdd_lora2
- C19 pad 2: Net-(D6-A) -> recovery
- C2 pad 1: Net-(J3-CRD) -> GND
- C2 pad 2: GND -> Net-(D1-A)
- C22 pad 2: Net-(U8-ANT) -> recovery
- C23 pad 2: Net-(U9-ANT) -> recovery
- C24 pad 2: Net-(J7-In) -> recovery
- C25 pad 2: Net-(J8-In) -> +3.3V
- C26 pad 2: vdd_lora1 -> +5V
- C27 pad 2: vdd_lora2 -> +3.3V
- C28 pad 1: GND -> ADC_RECOVERY_CURRENT
- C28 pad 2: vdd_lora1 -> GND
- C29 pad 2: vdd_lora2 -> +3.3V
- C3 pad 1: vdd_ethernet -> GND
- C3 pad 2: GND -> main
- C30 pad 2: main -> +5V
- C31 pad 2: recovery -> ADC_CONT_CHECK
- C32 pad 2: main -> Net-(U11-ANT)
- C33 pad 2: recovery -> Net-(J6-In)
- C34 pad 1: GND -> Net-(J8-CRD)
- C34 pad 2: recovery -> GND
- C35 pad 1: GND -> Net-(J8-CRD)
- C35 pad 2: main -> GND
- C36 pad 1: GND -> Net-(J8-CRD)
- C36 pad 2: recovery -> GND
- C37 pad 1: GND -> Net-(J8-CRD)
- C37 pad 2: +5V -> GND
- C38 pad 1: GND -> Net-(J8-CRD)
- C38 pad 2: +3.3V -> GND
- C39 pad 1: GND -> Net-(J8-CRD)
- C39 pad 2: +5V -> GND
- C4 pad 1: Net-(J3-CRD) -> GND
- C4 pad 2: GND -> main
- C40 pad 1: GND -> Net-(J8-CRD)
- C40 pad 2: main -> GND
- C43 pad 2: vdd_ethernet -> vdd_lora1
- C44 pad 2: +5V -> vdd_lora1
- C45 pad 1: GND -> vdd_ethernet
- C45 pad 2: +5V -> GND
- C46 pad 2: vdd_lora1 -> Net-(U13-ANT)
- C47 pad 2: vdd_lora2 -> Net-(J7-In)
- C5 pad 1: Net-(U1-VDDCR) -> GND
- C5 pad 2: GND -> main
- C51 pad 2: +3.3V -> Net-(C51-Pad2)
- C52 pad 2: recovery -> +5V
- C55 pad 2: recovery -> +5V
- C6 pad 1: Net-(J3-CRD) -> GND
- C6 pad 2: GND -> main
- C7 pad 1: Net-(U1-VDDCR) -> GND
- C7 pad 2: GND -> +5V
- C8 pad 1: Net-(J3-CRD) -> GND
- C8 pad 2: GND -> +3.3V
- C9 pad 1: Net-(J3-CRD) -> GND
- C9 pad 2: GND -> +5V
- D1 pad 1: UART4_RX_GPS -> +5V
- D1 pad 2: GND -> Net-(D1-A)
- D15 pad 1: main_pre_sense -> +5V
- D15 pad 2: recovery -> Net-(BZ1-+)
- D16 pad 1: +5V -> /Recovery Output Pair 1/out1_low
- D16 pad 2: Net-(BZ1-+) -> Net-(D16-A)
- D18 pad 1: GND -> /Recovery Output Pair 2/out1_low
- D2 pad 1: UART4_TX_GPS -> Net-(D2-K)
- D2 pad 2: GND -> recovery
- D3 pad 1: GPS_RESET -> Net-(D2-K)
- D3 pad 2: GND -> bus_main
- D4 pad 1: GPS_SAFEBOOT -> GND
- D4 pad 2: GND -> Net-(D4-A)
- D5 pad 1: +5V -> GND
- D6 pad 1: +5V -> GND
- D7 pad 1: GND -> +5V
- F1 pad 1: Net-(D19-K) -> Net-(J3-Pin_6)
- F1 pad 2: Net-(Q12-D) -> bus_main
- F2 pad 1: Net-(D20-K) -> /Recovery Output Pair 1/out1_high
- F2 pad 2: Net-(Q13-D) -> /Recovery Output Pair 1/recovery_high
- F3 pad 2: Net-(D13-K) -> /Recovery Output Pair 1/recovery_high
- F4 pad 1: Net-(Q11-D) -> /Recovery Output Pair 2/out1_high
- F4 pad 2: Net-(D17-K) -> /Recovery Output Pair 1/recovery_high
- F5 pad 2: bus_main -> /Recovery Output Pair 1/recovery_high
- FB1 pad 2: Net-(J3-CRD) -> Net-(J8-CRD)
- J1 pad 31: ETH_RXD0 -> ETH_RXD-
- J1 pad 32: ETH_RXD1 -> ETH_RXD+
- J1 pad 39: UART4_RX_GPS -> UART4_RX
- J1 pad 4: UART8_RX -> UART8_RX_GPS
- J1 pad 40: UART4_TX_GPS -> UART4_TX
- J1 pad 5: UART8_TX -> UART8_TX_GPS
- J2 pad 8: UART4_TX_GPS -> UART8_TX_GPS
- J2 pad 9: UART4_RX_GPS -> UART8_RX_GPS
- J3 pad 1: /TXP -> GND
- J3 pad 2: /TXN -> GND
- J3 pad 3: /RXP -> CAN1-
- J3 pad 4: Net-(J3-CRD) -> CAN2-
- J3 pad 5: Net-(J3-CRD) -> bus_supply
- J3 pad 6: /RXN -> Net-(J3-Pin_6)
- J3 pad 7: unconnected-(J3-NC-Pad7) -> CAN1+
- J3 pad 8: GND -> CAN2+
- J5 pad 3: CAN_1_L -> /Recovery Output Pair 1/out1_low
- J5 pad 4: CAN_2_L -> /Recovery Output Pair 1/out2_low
- J5 pad 5: charging_voltage -> /Recovery Output Pair 2/out1_low
- J5 pad 6: Net-(D14-A) -> /Recovery Output Pair 2/out2_low
- J5 pad 7: CAN_1_H -> recovery
- J5 pad 8: CAN_2_H -> recovery
- J6 pad 1: GND -> Net-(J6-In)
- J8 pad 1: Net-(J8-In) -> /TXP
- J8 pad 2: GND -> /TXN
- Q1 pad 1: Net-(Q1-G) -> recovery
- Q1 pad 2: GND -> recovery
- Q1 pad 3: Net-(BZ1-+) -> recovery
- Q8 pad 1: Net-(Q8-G) -> (no net)
- Q8 pad 2: GND -> (no net)
- Q8 pad 3: Net-(Q8-D) -> GND
- R1 pad 1: Net-(U1-RXD0/MODE0) -> Net-(D2-K)
- R1 pad 2: ETH_RXD- -> main
- R10 pad 1: Net-(U1-RXD1/MODE1) -> recovery
- R10 pad 2: vdd_ethernet -> Net-(D6-A)
- R11 pad 1: Net-(U1-RXD0/MODE0) -> Net-(D7-A)
- R11 pad 2: vdd_ethernet -> Net-(D8-A)
- R13 pad 1: Net-(J3-CRD) -> CAN1+
- R13 pad 2: /TXP -> Net-(JP3-B)
- R14 pad 1: Net-(J3-CRD) -> RECOVERY_HIGH
- R14 pad 2: /TXN -> Net-(Q2-G)
- R15 pad 1: Net-(U1-RBIAS) -> Net-(Q2-G)
- R16 pad 1: Net-(J3-CRD) -> +3.3V
- R16 pad 2: /RXP -> Net-(Q3-G)
- R17 pad 1: Net-(J3-CRD) -> Net-(D9-K)
- R17 pad 2: /RXN -> /Recovery Output Pair 1/recovery_high
- R19 pad 1: bus_main -> /Recovery Output Pair 1/recovery_high
- R19 pad 2: ADC_BUS_MAIN_VOLTAGE -> Net-(D10-A)
- R2 pad 1: Net-(U1-RXD1/MODE1) -> bus_main
- R2 pad 2: ETH_RXD+ -> ADC_BUS_MAIN_VOLTAGE
- R20 pad 1: ADC_BUS_MAIN_VOLTAGE -> Net-(Q3-S)
- R20 pad 2: GND -> Net-(R20-Pad2)
- R21 pad 1: Net-(U1-XTAL1/CLKIN) -> Net-(R20-Pad2)
- R21 pad 2: Net-(C12-Pad2) -> Net-(D9-A)
- R22 pad 1: Net-(U1-LED2/~{INTSEL}) -> CAN2+
- R22 pad 2: GND -> Net-(JP4-B)
- R25 pad 1: bus_supply -> Net-(U14-~{INT}/REFCLKO)
- R25 pad 2: ADC_BUS_SUPPLY_VOLTAGE -> vdd_ethernet
- R26 pad 1: ADC_BUS_SUPPLY_VOLTAGE -> Net-(U14-MDIO)
- R26 pad 2: GND -> vdd_ethernet
- R27 pad 1: Net-(C13-Pad2) -> Net-(U14-CRS_DV/MODE2)
- R27 pad 2: Net-(U1-XTAL2) -> vdd_ethernet
- R28 pad 1: recovery -> Net-(U14-RXD1/MODE1)
- R28 pad 2: ADC_RECOVERY_VOLTAGE -> vdd_ethernet
- R29 pad 1: Net-(J3-Pad10) -> Net-(U14-RXD0/MODE0)
- R29 pad 2: GND -> vdd_ethernet
- R3 pad 1: Net-(U1-RXER/PHYAD0) -> bus_supply
- R3 pad 2: GND -> ADC_BUS_SUPPLY_VOLTAGE
- R34 pad 1: Net-(D5-A) -> Net-(U13-ANT)
- R34 pad 2: Net-(D7-A) -> Net-(J7-In)
- R35 pad 1: Net-(D6-A) -> Net-(U14-RXD0/MODE0)
- R35 pad 2: Net-(D8-A) -> ETH_RXD-
- R38 pad 1: Net-(U8-ANT) -> Net-(U14-CRS_DV/MODE2)
- R38 pad 2: Net-(J7-In) -> ETH_RMII_CRS_DV
- R39 pad 1: Net-(U9-ANT) -> Net-(U14-MDIO)
- R39 pad 2: Net-(J8-In) -> ETH_MDIO
- R4 pad 1: Net-(U1-CRS_DV/MODE2) -> recovery
- R4 pad 2: ETH_RMII_CRS_DV -> ADC_RECOVERY_VOLTAGE
- R40 pad 1: CAN1+ -> Net-(U14-RBIAS)
- R40 pad 2: CAN1- -> GND
- R41 pad 1: CAN2+ -> DAC
- R41 pad 2: CAN2- -> Net-(J9-Pin_2)
- R42 pad 1: ADC_RECOVERY_VOLTAGE -> ADC_IN
- R42 pad 2: GND -> Net-(J9-Pin_3)
- R43 pad 1: BUZZER -> Net-(U14-~{INT}/REFCLKO)
- R43 pad 2: GND -> ETH_REF_CLK
- R44 pad 2: Net-(Q1-G) -> Net-(Q4-G)
- R48 pad 1: /Recovery Output 1 & 2/recovery_high -> BUZZER
- R48 pad 2: Net-(D18-A) -> GND
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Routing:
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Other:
- board size 70 x 120 mm -> 85.8 x 120 mm
- board text added: "BUS"
- board text added: "REC"
- board text removed: "@TODO check if footprint is correct"
